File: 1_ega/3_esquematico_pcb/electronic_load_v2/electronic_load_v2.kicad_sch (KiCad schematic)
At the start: 65 parts, among them J1 Encoder, J10 5V, J11 LOAD, J12 Memoria SD, J13 LCD, J14 Io_sens, J15 VCC, J17 EGB_I2C, J18 EGB_UART, J2 RTC_I2C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

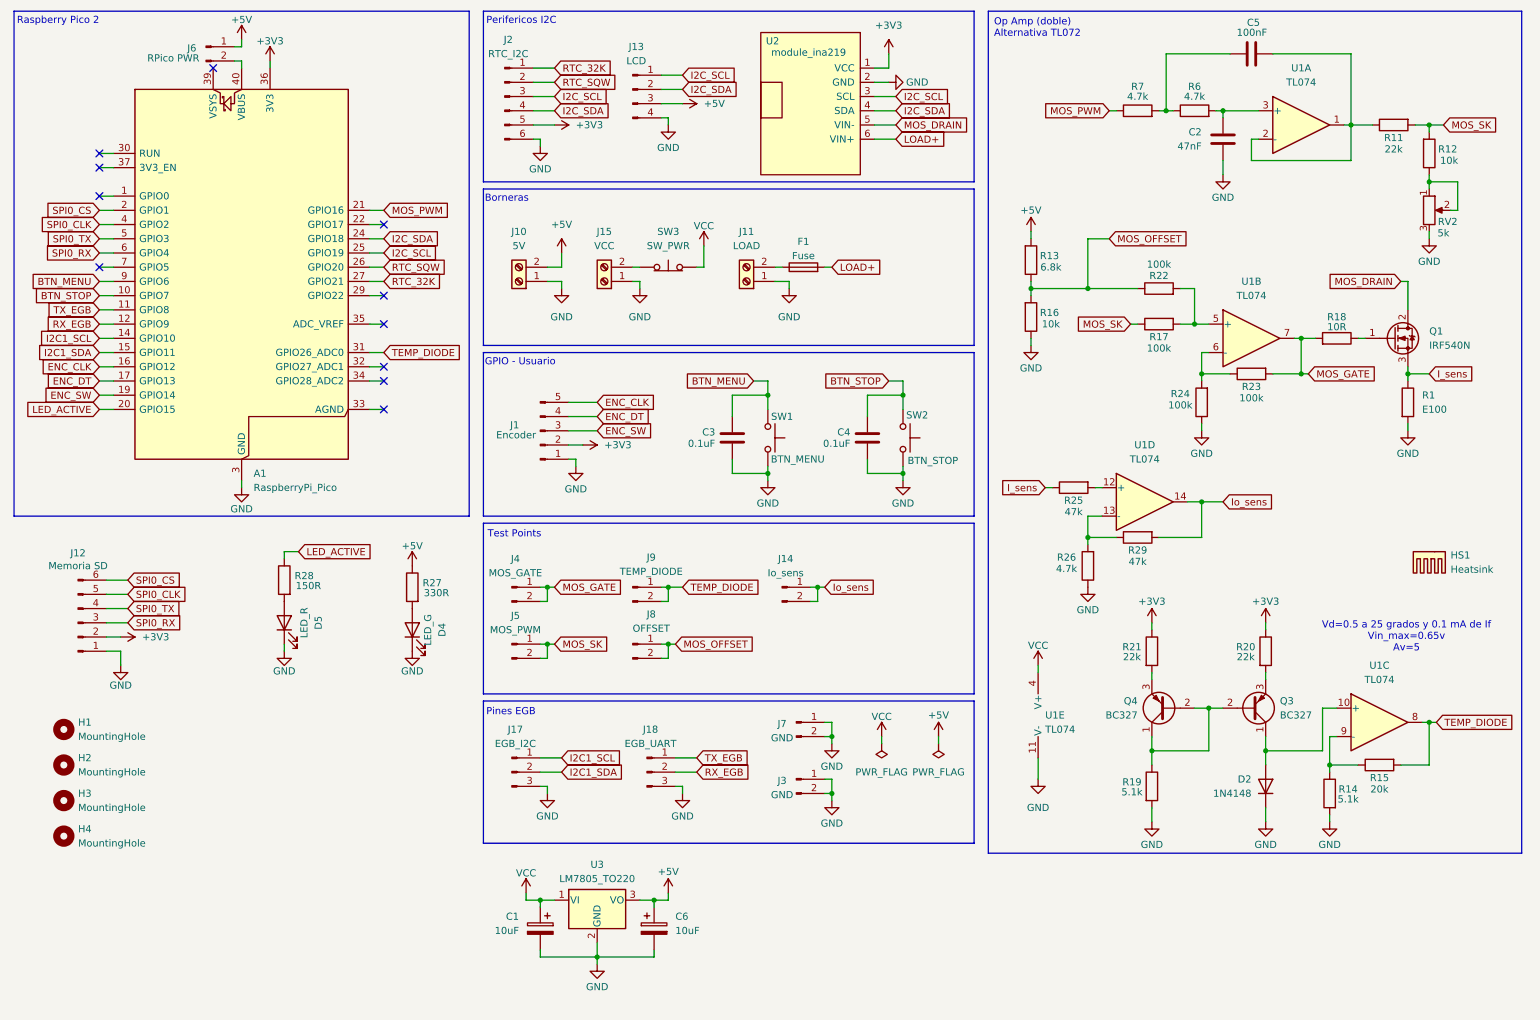
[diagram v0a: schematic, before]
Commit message: chore: pwm_offset con gpio
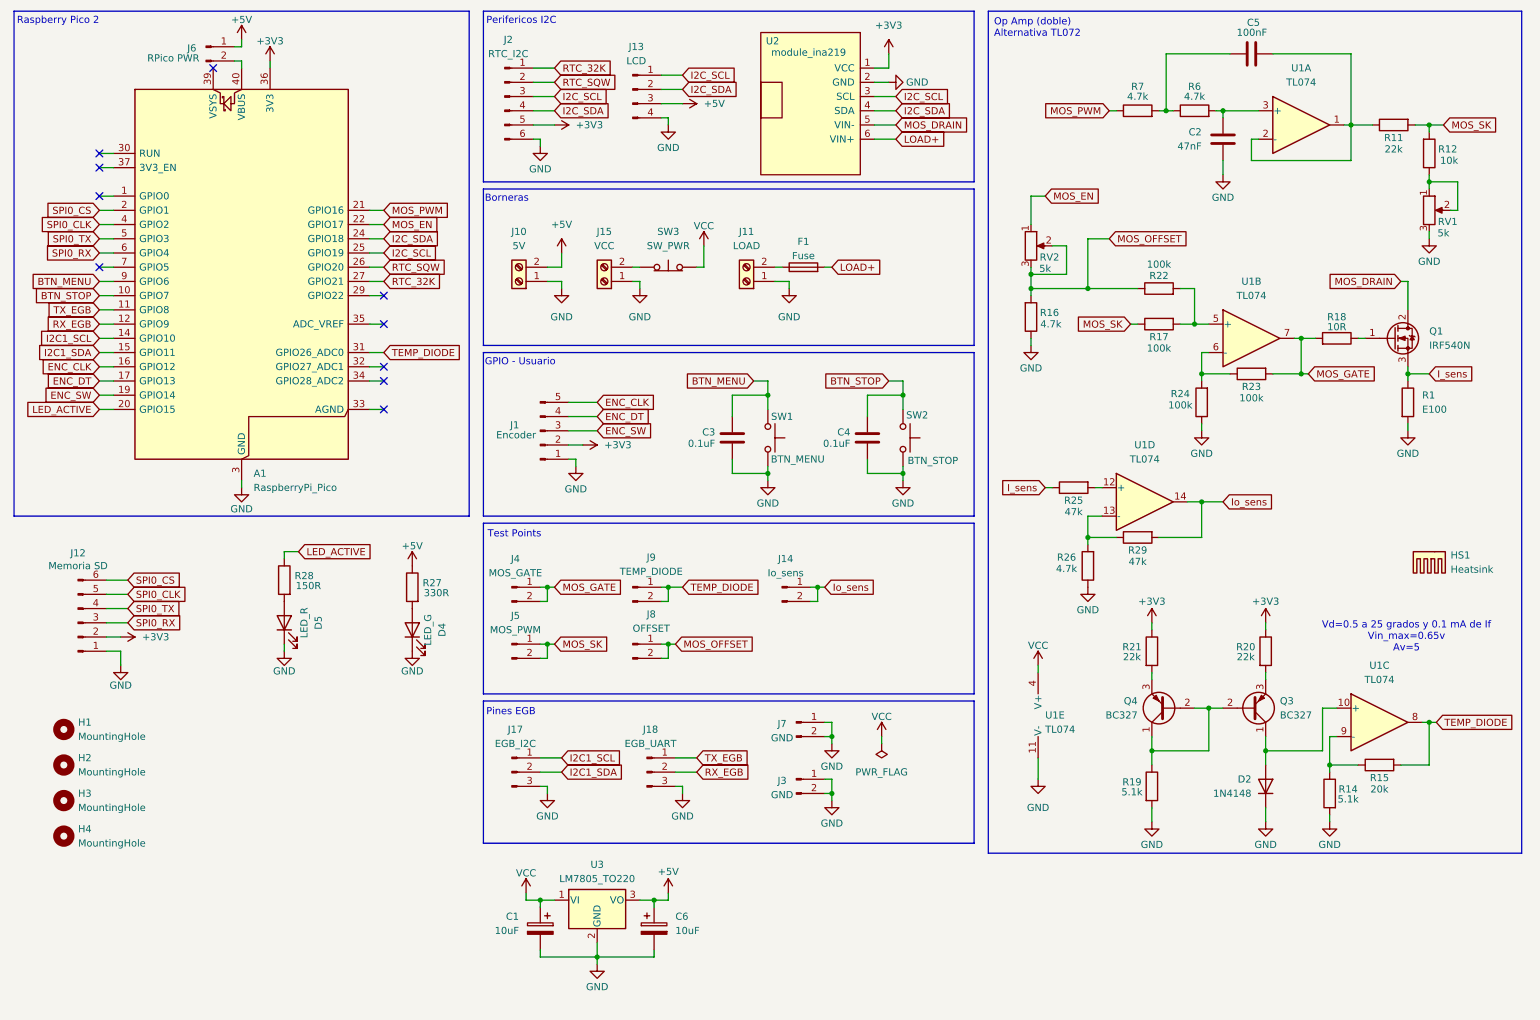
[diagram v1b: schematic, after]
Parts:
- removed R13: 6.8k, Resistor_THT:R_Axial_DIN0207_L6.3mm_D2.5mm_P10.16mm_Horizontal, symbol Device:R
- added RV2: 5k, Connector_PinHeader_2.54mm:PinHeader_1x03_P2.54mm_Vertical, symbol Device:R_Potentiometer
- R16: value 10k -> 4.7k
- renumbered RV2 to RV1
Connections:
- net MOS_OFFSET: now also RV2.2, RV2.3
- net MOS_EN: now reaches A1.22 (GPIO17)
- net MOS_EN: now also RV2.1
- no-connect marks 11 -> 10

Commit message: perf: resistencias a huellas smd y preliminar de segunda version de pcb
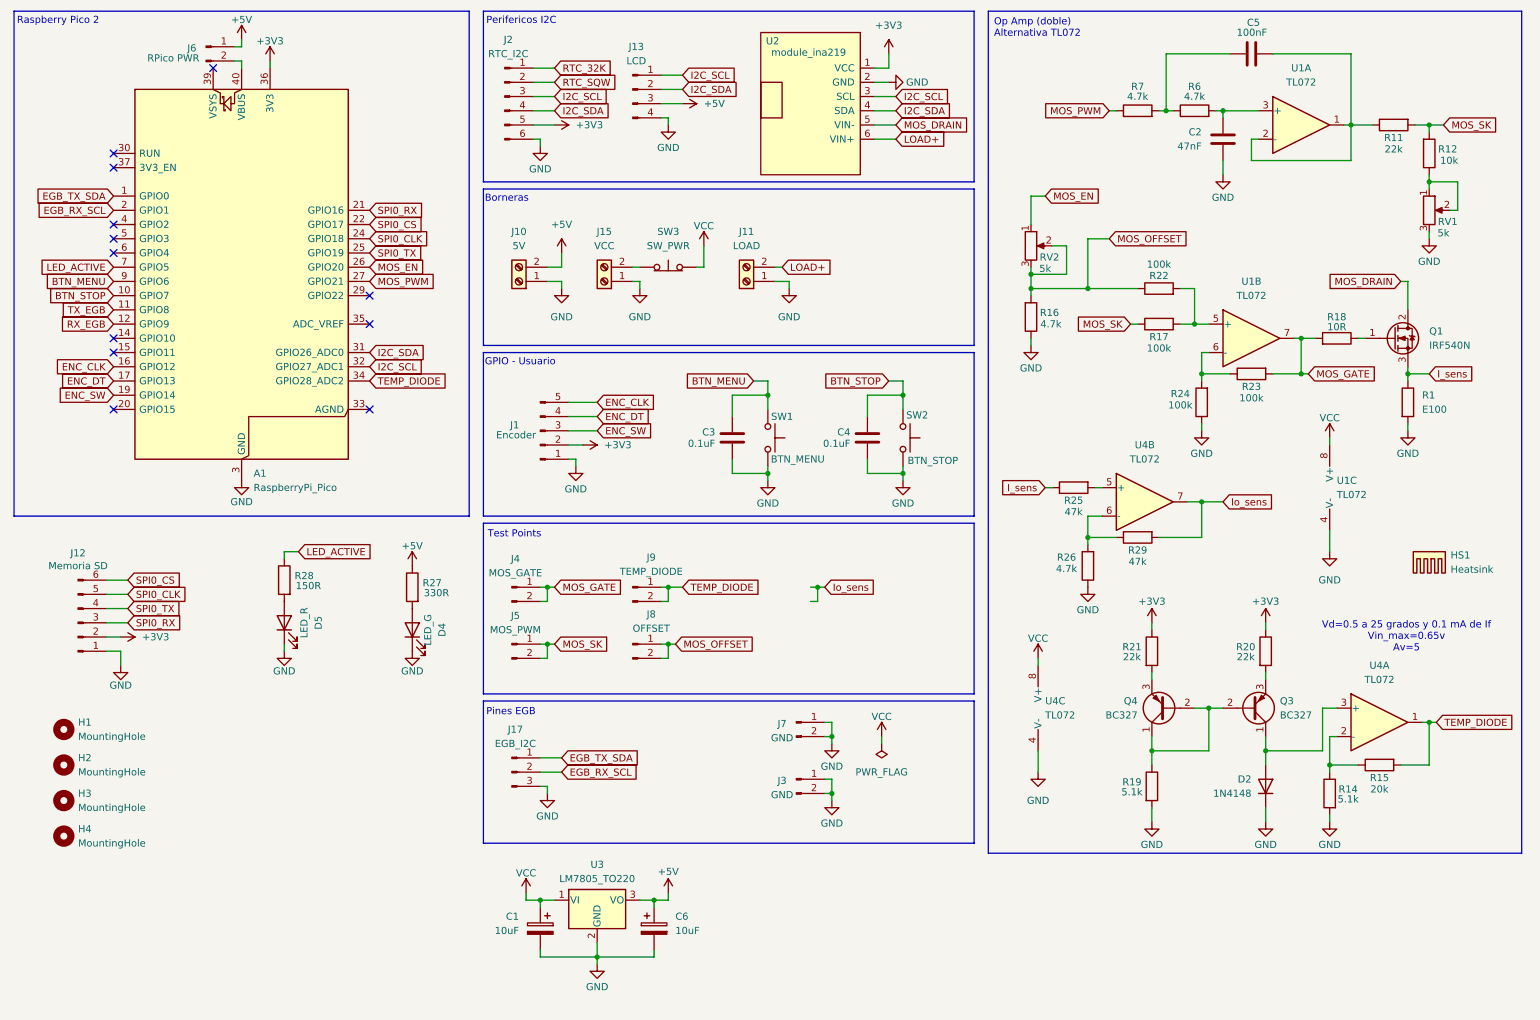
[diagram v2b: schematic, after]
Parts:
- removed F1: Fuse, Fuse:Fuseholder_Clip-5x20mm_Eaton_1A5601-01_Inline_P20.80x6.76mm_D1.70mm_Horizontal, symbol Device:Fuse
- removed J14: Io_sens, Connector_PinHeader_2.54mm:PinHeader_1x02_P2.54mm_Vertical, symbol Connector:Conn_01x02_Pin
- removed J18: EGB_UART, Connector_PinSocket_2.54mm:PinSocket_1x03_P2.54mm_Vertical, symbol Connector:Conn_01x03_Pin
- removed U1: TL074, Package_DIP:DIP-14_W7.62mm_Socket_LongPads, symbol Amplifier_Operational:TL074
- added U1, U4: TL072, Package_DIP:DIP-8_W7.62mm_LongPads, symbol Amplifier_Operational:TL072
- C2, C5: footprint Capacitor_THT:C_Disc_D5.0mm_W2.5mm_P5.00mm -> Capacitor_SMD:C_0805_2012Metric_Pad1.18x1.45mm_HandSolder
- C3, C4: footprint Capacitor_THT:C_Disc_D3.4mm_W2.1mm_P2.50mm -> Capacitor_SMD:C_0805_2012Metric_Pad1.18x1.45mm_HandSolder
- D4, D5: footprint LED_THT:LED_D3.0mm -> LED_THT:LED_D5.0mm
- Q1: footprint Package_TO_SOT_THT:TO-220-3_Vertical -> Package_TO_SOT_THT:TO-220F-3_Horizontal_TabUp
- R1: footprint Resistor_THT:R_Axial_Power_L20.0mm_W6.4mm_P25.40mm -> Resistor_THT:R_Axial_DIN0309_L9.0mm_D3.2mm_P12.70mm_Horizontal
- R11, R12, R14, R15, R16, R17, R18, R19, R20, R21, R22, R23, R24, R25, R26, R27, R28, R29, R6, R7: footprint Resistor_THT:R_Axial_DIN0207_L6.3mm_D2.5mm_P10.16mm_Horizontal -> Resistor_SMD:R_0805_2012Metric_Pad1.20x1.40mm_HandSolder
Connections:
- net GND: now also U1.4 (V-), U4.4 (V-)
- net I2C_SCL: now also A1.32 (GPIO27_ADC1); no longer A1.25 (GPIO19)
- net I2C_SDA: now also A1.31 (GPIO26_ADC0); no longer A1.24 (GPIO18)
- net Io_sens: now also U4.7
- net LED_ACTIVE: now also A1.7 (GPIO5); no longer A1.20 (GPIO15)
- net LOAD+: now also J11.2 (Pin_2)
- net MOS_EN: now also A1.26 (GPIO20); no longer A1.22 (GPIO17)
- net MOS_GATE: now also U1.7
- net MOS_PWM: now also A1.27 (GPIO21); no longer A1.21 (GPIO16)
- net RTC_32K: no longer A1.27 (GPIO21)
- net RTC_SQW: no longer A1.26 (GPIO20)
- net SPI0_CLK: now also A1.24 (GPIO18); no longer A1.4 (GPIO2)
- net SPI0_CS: now also A1.22 (GPIO17); no longer A1.2 (GPIO1)
- net SPI0_RX: now also A1.21 (GPIO16); no longer A1.6 (GPIO4)
- net SPI0_TX: now also A1.25 (GPIO19); no longer A1.5 (GPIO3)
- net TEMP_DIODE: now also A1.34 (GPIO28_ADC2), U4.1; no longer A1.31 (GPIO26_ADC0)
- net VCC: now also U1.8 (V+), U4.8 (V+)
- net at C2.1, R6.2: now also U1.3 (+)
- net at R25.2: now also U4.5 (+)
- net at R26.2, R29.1: now also U4.6 (-)
- net at R23.1, R24.2: now also U1.6 (-)
- net at R14.1, R15.1: now also U4.2 (-)
- net at D2.2 (A), Q3.1 (C): now also U4.3 (+)
- net at C5.2, R11.1: now also U1.1, U1.2 (-)
- net at R17.2, R22.2: now also U1.5 (+)
- net EGB_TX_SDA: now reaches A1.1 (GPIO0)
- net EGB_TX_SDA: now also J17.1 (Pin_1)
- net I2C1_SCL: no longer names the net of A1.14 (GPIO10)
- net I2C1_SCL: no longer J17.1 (Pin_1)
- net I2C1_SDA: no longer names the net of A1.15 (GPIO11)
- net I2C1_SDA: no longer J17.2 (Pin_2)
- new net EGB_RX_SCL: A1.2 (GPIO1), J17.2 (Pin_2)
- no-connect marks 10 -> 12

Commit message: chore: pcb v1 10x5 con R y C smd. INA modulo
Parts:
- removed C6: 10uF, Capacitor_THT:CP_Radial_D6.3mm_P2.50mm, symbol Device:C_Polarized
- removed D5: LED_R, LED_THT:LED_D5.0mm, symbol Device:LED
- removed J10: 5V, TerminalBlock_Phoenix:TerminalBlock_Phoenix_MKDS-1,5-2-5.08_1x02_P5.08mm_Horizontal, symbol Connector:Screw_Terminal_01x02
- removed J2: RTC_I2C, Connector_PinSocket_2.54mm:PinSocket_1x06_P2.54mm_Vertical, symbol Connector:Conn_01x06_Pin
- removed J4: MOS_GATE, Connector_PinHeader_2.54mm:PinHeader_1x02_P2.54mm_Vertical, symbol Connector:Conn_01x02_Pin
- removed J5: MOS_PWM, Connector_PinHeader_2.54mm:PinHeader_1x02_P2.54mm_Vertical, symbol Connector:Conn_01x02_Pin
- removed J9: TEMP_DIODE, Connector_PinHeader_2.54mm:PinHeader_1x02_P2.54mm_Vertical, symbol Connector:Conn_01x02_Pin
- removed R28: 150R, Resistor_SMD:R_0805_2012Metric_Pad1.20x1.40mm_HandSolder, symbol Device:R
- removed U1, U4: TL072, Package_DIP:DIP-8_W7.62mm_LongPads, symbol Amplifier_Operational:TL072
- added C6: 100nF, Capacitor_SMD:C_0805_2012Metric_Pad1.18x1.45mm_HandSolder, symbol Device:C
- added C7: 330nF, Capacitor_SMD:C_0805_2012Metric_Pad1.18x1.45mm_HandSolder, symbol Device:C
- added J16: RTC, Connector_PinHeader_2.54mm:PinHeader_1x04_P2.54mm_Vertical, symbol Connector:Conn_01x04_Pin
- added R30: 3.3k, Resistor_SMD:R_1206_3216Metric_Pad1.30x1.75mm_HandSolder, symbol Device:R
- added TP1: MOS_GATE, Connector_Pin:Pin_D0.7mm_L6.5mm_W1.8mm_FlatFork, symbol Connector:TestPoint
- added TP2: MOS_SK, Connector_Pin:Pin_D0.7mm_L6.5mm_W1.8mm_FlatFork, symbol Connector:TestPoint
- added TP3: MOS_OFFSET, Connector_Pin:Pin_D0.7mm_L6.5mm_W1.8mm_FlatFork, symbol Connector:TestPoint
- added TP4: T_DIODE, Connector_Pin:Pin_D0.7mm_L6.5mm_W1.8mm_FlatFork, symbol Connector:TestPoint
- added TP5: Isense, Connector_Pin:Pin_D0.7mm_L6.5mm_W1.8mm_FlatFork, symbol Connector:TestPoint
- added U1: LM324, Package_DIP:DIP-14_W7.62mm_Socket, symbol Amplifier_Operational:LM324
- C1: value 10uF -> 100uF; footprint Capacitor_THT:CP_Radial_D6.3mm_P2.50mm -> Capacitor_THT:CP_Radial_D5.0mm_P2.50mm
- J8: value OFFSET -> 5V
- Q1: footprint Package_TO_SOT_THT:TO-220F-3_Horizontal_TabUp -> Package_TO_SOT_THT:TO-220-3_Vertical
- R11, R12, R14, R15, R16, R17, R18, R19, R22, R23, R24, R25, R26, R27, R29, R6, R7: footprint Resistor_SMD:R_0805_2012Metric_Pad1.20x1.40mm_HandSolder -> Resistor_SMD:R_1206_3216Metric_Pad1.30x1.75mm_HandSolder
- R20, R21: footprint Resistor_SMD:R_0805_2012Metric_Pad1.20x1.40mm_HandSolder -> Resistor_THT:R_Axial_DIN0207_L6.3mm_D2.5mm_P10.16mm_Horizontal
- RV1, RV2: footprint Connector_PinHeader_2.54mm:PinHeader_1x03_P2.54mm_Vertical -> Potentiometer_THT:Potentiometer_Bourns_3296W_Vertical
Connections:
- net LED_ACTIVE is gone; now on net SPI0_RX: A1.7 (GPIO5)
- net TX_EGB is gone; now on net SPI0_CS: A1.11 (GPIO8)
- net +3V3: now also J1.4 (Pin_4), J16.3 (Pin_3); no longer J1.2 (Pin_2)
- net +5V: now also J8.1 (Pin_1), J8.2 (Pin_2), C6.2
- net BTN_MENU: now also A1.4 (GPIO2); no longer A1.9 (GPIO6)
- net BTN_STOP: now also A1.6 (GPIO4); no longer A1.10 (GPIO7)
- net EGB_RX_SCL: now also J17.1 (Pin_1); no longer J17.2 (Pin_2)
- net EGB_TX_SDA: now also J17.2 (Pin_2); no longer J17.1 (Pin_1)
- net ENC_CLK: now also A1.20 (GPIO15), J1.1 (Pin_1); no longer A1.16 (GPIO12), J1.5 (Pin_5)
- net ENC_DT: now also A1.19 (GPIO14), J1.2 (Pin_2); no longer A1.17 (GPIO13), J1.4 (Pin_4)
- net ENC_SW: now also A1.17 (GPIO13); no longer A1.19 (GPIO14)
- net GND: now also A1.33 (AGND), J1.5 (Pin_5), RV2.3, C6.1, C7.1, J16.4 (Pin_4), U1.11 (V-); no longer J1.1 (Pin_1), R16.1
- net I2C_SCL: now also A1.25 (GPIO19), J16.1 (Pin_1); no longer A1.32 (GPIO27_ADC1)
- net I2C_SDA: now also A1.24 (GPIO18), J16.2 (Pin_2); no longer A1.31 (GPIO26_ADC0)
- net Io_sens: now also TP5.1, U1.8
- net MOS_EN: now also A1.21 (GPIO16), R16.2; no longer A1.26 (GPIO20), RV2.1
- net MOS_GATE: now also TP1.1, U1.14
- net MOS_OFFSET: now also R16.1, R30.2, TP3.1; no longer J8.1 (Pin_1), J8.2 (Pin_2), R16.2, RV2.2, RV2.3
- net MOS_PWM: now also A1.22 (GPIO17); no longer A1.27 (GPIO21)
- net MOS_SK: now also TP2.1
- net SPI0_CLK: now also A1.9 (GPIO6); no longer A1.24 (GPIO18)
- net SPI0_CS: now also J12.3 (Pin_3); no longer A1.22 (GPIO17), J12.6 (Pin_6)
- net SPI0_RX: now also J12.6 (Pin_6); no longer A1.21 (GPIO16), J12.3 (Pin_3)
- net SPI0_TX: now also A1.10 (GPIO7); no longer A1.25 (GPIO19)
- net TEMP_DIODE: now also A1.31 (GPIO26_ADC0), TP4.1, U1.7; no longer A1.34 (GPIO28_ADC2)
- net VCC: now also C7.2, U1.4 (V+)
- net at C2.1, R6.2: now also U1.3 (+)
- net at R23.1, R24.2: now also U1.13 (-)
- net at R26.2, R29.1: now also U1.9 (-)
- net at R14.1, R15.1: now also U1.6 (-)
- net at D2.2 (A), Q3.1 (C): now also U1.5 (+)
- net at R17.2, R22.2: now also U1.12 (+)
- net at C5.2, R11.1: now also U1.1, U1.2 (-)
- net at R25.2: now also U1.10 (+)
- net RX_EGB: no longer names the net of A1.12 (GPIO9)
- new net: R30.1, RV2.1, RV2.2
- no-connect marks 12 -> 14
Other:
- moved on the sheet: C1, J11, J15, J7, R16, RV2, SW3, U3
